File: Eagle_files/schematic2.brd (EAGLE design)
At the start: 101.6 x 53.3 mm, 77 parts, among them IC6 DS3231/SO

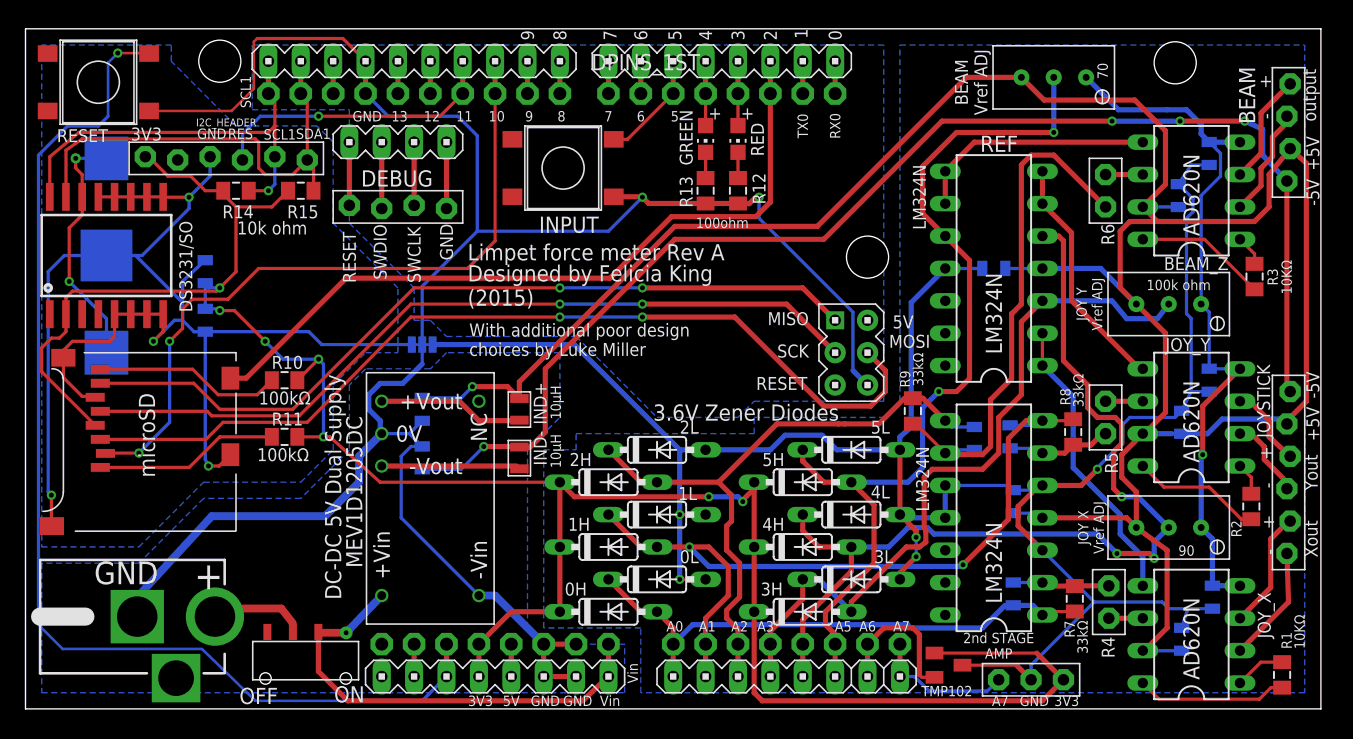
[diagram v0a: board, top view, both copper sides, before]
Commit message: Aligned all of the diodes to make a little more room. Increased the spacing between the analog ground plane and the neighboring planes. Rewired the A7 analog header so it conforms to standard TMP35, LM35 style temperature sensor pinouts. Swapped the gain-setting resistors on the In-AMPS to 2-pin header style so that we can swap resistors easily to change gain.
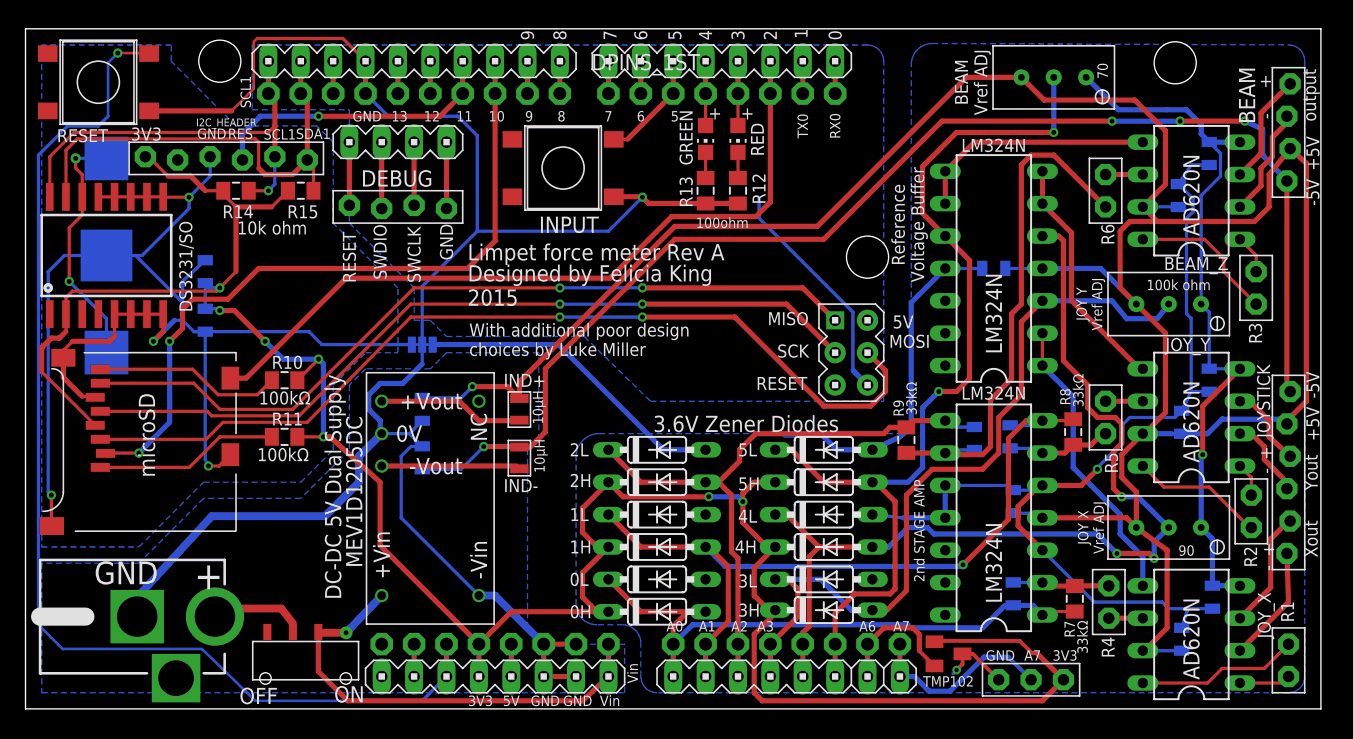
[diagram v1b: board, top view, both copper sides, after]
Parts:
- R1, R2, R3: value 10KΩ -> (none); device Felicia_force_logger:R0805 -> Felicia_force_logger:1X02
- moved 0H 3.81 mm to (49.5, 7.62)
- moved 1H 3.81 mm to (49.5, 12.7)
- moved 2H 3.81 mm to (49.5, 17.8)
- moved R9 2.34 mm to (69.1, 21.1)
- moved 3L 2.16 mm to (62.6, 10.2)
- moved 4L 2.16 mm to (62.6, 15.2)
- moved 5L 2.16 mm to (62.6, 20.3)
- moved 3H 1.66 mm to (62.6, 7.75)
- moved 4H 1.65 mm to (62.6, 12.7)
- moved 5H 1.65 mm to (62.6, 17.8)
- moved R1 1.25 mm to (99.1, 3.81), turned to 270 degrees
- moved R3 0.90 mm to (96.5, 33.0)
- moved TMP102 0.89 mm to (72.4, 4.32)
- moved R2 0.38 mm to (96.1, 15.5)
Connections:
- net A7: now also ANALOG7_HEADER.2; no longer ANALOG7_HEADER.1
- net AGND: now also ANALOG7_HEADER.1; no longer ANALOG7_HEADER.2
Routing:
- net AGND: track 174.5 -> 135.2 mm, vias 5 -> 2
- net +3V3: track 180.0 -> 190.4 mm
- net A3: track 58.3 -> 62.3 mm
- net A7: track 11.1 -> 15.1 mm
- net A0: track 43.9 -> 47.6 mm
- net A5: track 72.9 -> 76.4 mm
- net GND: track 169.5 -> 167.6 mm, vias 2 -> 1
- net A6: track 11.8 -> 10.3 mm
- net N$10: track 10.4 -> 11.6 mm
- net A2: track 50.4 -> 49.5 mm
- net N$6: track 11.8 -> 12.7 mm
- net N$9: track 2.39 -> 3.07 mm
- net A1: vias 2 -> 1
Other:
- board text added: "Designed by Felicia King 2015"
- board text added: "Reference Voltage Buffer"
- board text removed: "A5"
- board text removed: "Designed by Felicia King (2015)"
